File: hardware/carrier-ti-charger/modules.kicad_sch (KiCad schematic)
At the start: 31 parts, among them J10 J_ADS_MAIN ADSBee J5, J11 J_ADS_GNSS ADSBee J4, J5 J_GNSS GPS-18037 J5, J6 J_ESP_A support, J7 J_ESP_B power/UART, J8 J_ESP_C I2C, J9 J_ESP_D support, U11 TPS259474LRPWR, U12 TPS259474LRPWR

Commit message: Refine resistors.
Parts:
- R73, R75: footprint carrier:R_0805_2012Metric_NoSilk -> Resistor_SMD:R_0603_1608Metric; LCSC C706247 -> C2924137; MPN RT0805BRD075K36L -> AR03BTCX5361A; Manufacturer YAGEO -> Viking Tech
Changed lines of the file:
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@@
 			)
 		)
-		(property "Footprint" "carrier:R_0805_2012Metric_NoSilk"
+		(property "Footprint" "Resistor_SMD:R_0603_1608Metric"
 			(at 54.61 78.74 0)
 			(hide yes)
@@
 			)
 		)
-		(property "Datasheet" "https://datasheet.lcsc.com/datasheet/pdf/46d7760c582640714d605308a25a220a.pdf?productCode=C706247"
+		(property "Datasheet" "https://datasheet.lcsc.com/datasheet/pdf/5bf30c62a4b85499d309118a7d825f44.pdf?productCode=C2924137"
 			(at 54.61 78.74 0)
 			(hide yes)
@@
 			)
 		)
-		(property "Description" "OVLO divider, 0.1%, 25 ppm/C, 125 mW, 150 V"
+		(property "Description" "OVLO divider, 0.1%, 25 ppm/C, 100 mW, 75 V"
 			(at 54.61 78.74 0)
 			(hide yes)
@@
 			)
 		)
-		(property "LCSC" "C706247"
+		(property "LCSC" "C2924137"
 			(at 54.61 78.74 0)
 			(hide yes)
@@
 			)
 		)
-		(property "MPN" "RT0805BRD075K36L"
+		(property "MPN" "AR03BTCX5361A"
 			(at 54.61 78.74 0)
 			(hide yes)
@@
 			)
 		)
-		(property "Manufacturer" "YAGEO"
+		(property "Manufacturer" "Viking Tech"
 			(at 54.61 78.74 0)
 			(hide yes)
@@
 			)
 		)
-		(property "Footprint" "carrier:R_0805_2012Metric_NoSilk"
+		(property "Footprint" "Resistor_SMD:R_0603_1608Metric"
 			(at 54.61 139.7 0)
 			(hide yes)
@@
 			)
 		)
-		(property "Datasheet" "https://datasheet.lcsc.com/datasheet/pdf/46d7760c582640714d605308a25a220a.pdf?productCode=C706247"
+		(property "Datasheet" "https://datasheet.lcsc.com/datasheet/pdf/5bf30c62a4b85499d309118a7d825f44.pdf?productCode=C2924137"
 			(at 54.61 139.7 0)
 			(hide yes)
@@
 			)
 		)
-		(property "Description" "OVLO divider, 0.1%, 25 ppm/C, 125 mW, 150 V"
+		(property "Description" "OVLO divider, 0.1%, 25 ppm/C, 100 mW, 75 V"
 			(at 54.61 139.7 0)
 			(hide yes)
@@
 			)
 		)
-		(property "LCSC" "C706247"
+		(property "LCSC" "C2924137"
 			(at 54.61 139.7 0)
 			(hide yes)
@@
 			)
 		)
-		(property "MPN" "RT0805BRD075K36L"
+		(property "MPN" "AR03BTCX5361A"
 			(at 54.61 139.7 0)
 			(hide yes)
@@
 			)
 		)
-		(property "Manufacturer" "YAGEO"
+		(property "Manufacturer" "Viking Tech"
 			(at 54.61 139.7 0)
 			(hide yes)

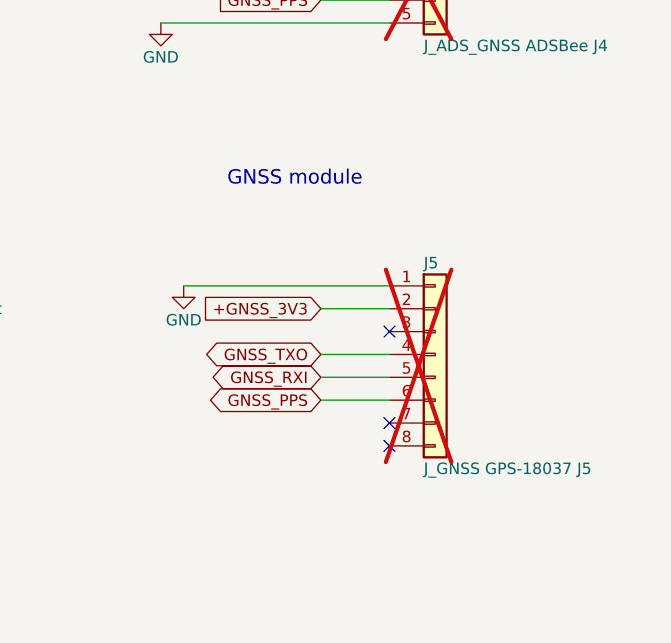
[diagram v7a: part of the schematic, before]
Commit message: Switch to Max M10 on-board chip instead of module.
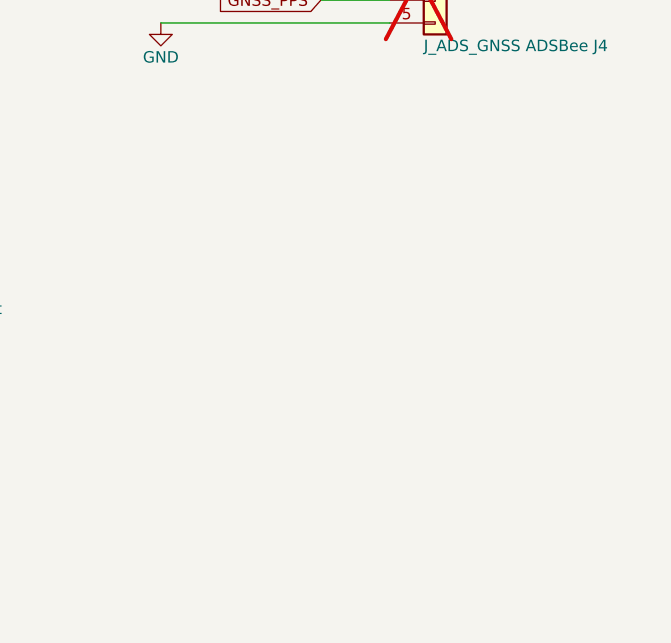
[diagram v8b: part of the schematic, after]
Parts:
- removed J5: J_GNSS GPS-18037 J5, Connector_PinSocket_2.54mm:PinSocket_1x08_P2.54mm_Vertical, symbol Connector_Generic:Conn_01x08
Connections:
- no-connect marks 24 -> 21
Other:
- note removed: "GNSS module"
